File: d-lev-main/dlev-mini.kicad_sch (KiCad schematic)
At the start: 41 parts, among them J1 Conn_01x12_MountingPin, J3 S8B-PH-SM4-TB, J4 S8B-PH-SM4-TB, J5 Conn_01x06_MountingPin, Q3 BSS138, Q4 BSS138, Q5 BSS138, U2 AMS1117-3.3, U4 25LCxxx

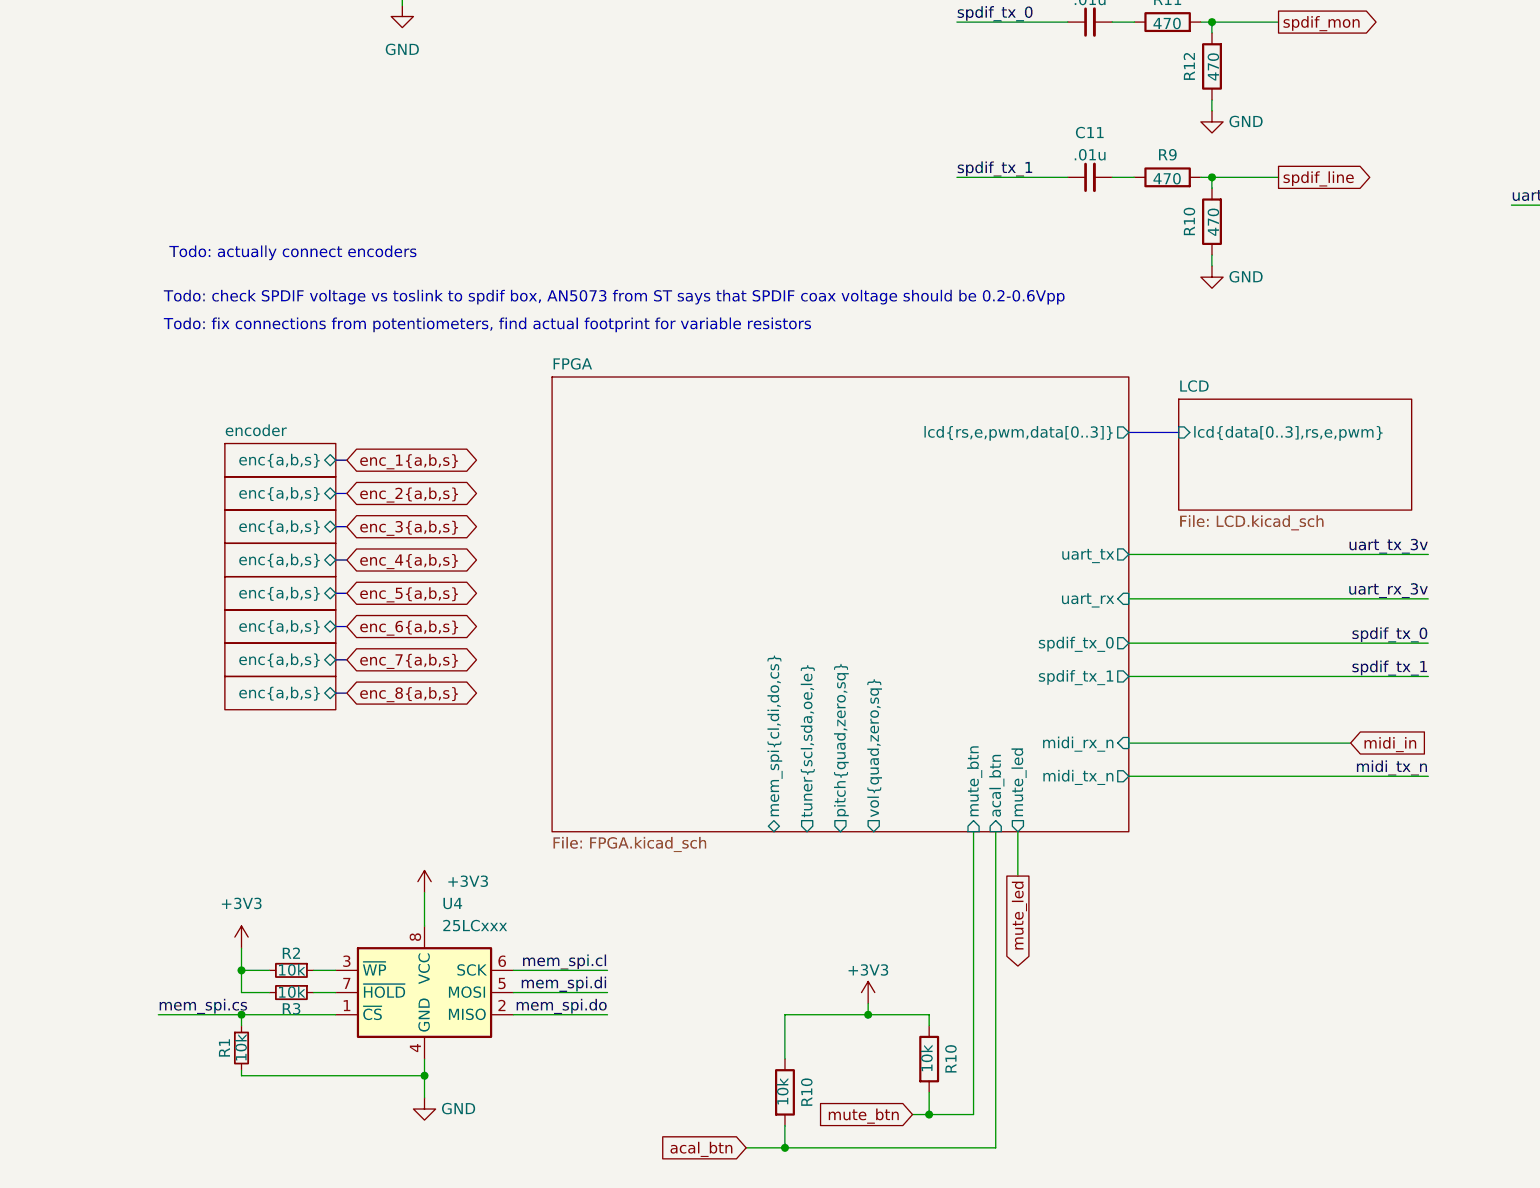
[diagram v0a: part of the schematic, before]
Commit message: start routing
* add simple knob model
* place encoders
* change display to use SMT female headers and SMTSO screw holes
* rotate fpga model 90 degrees
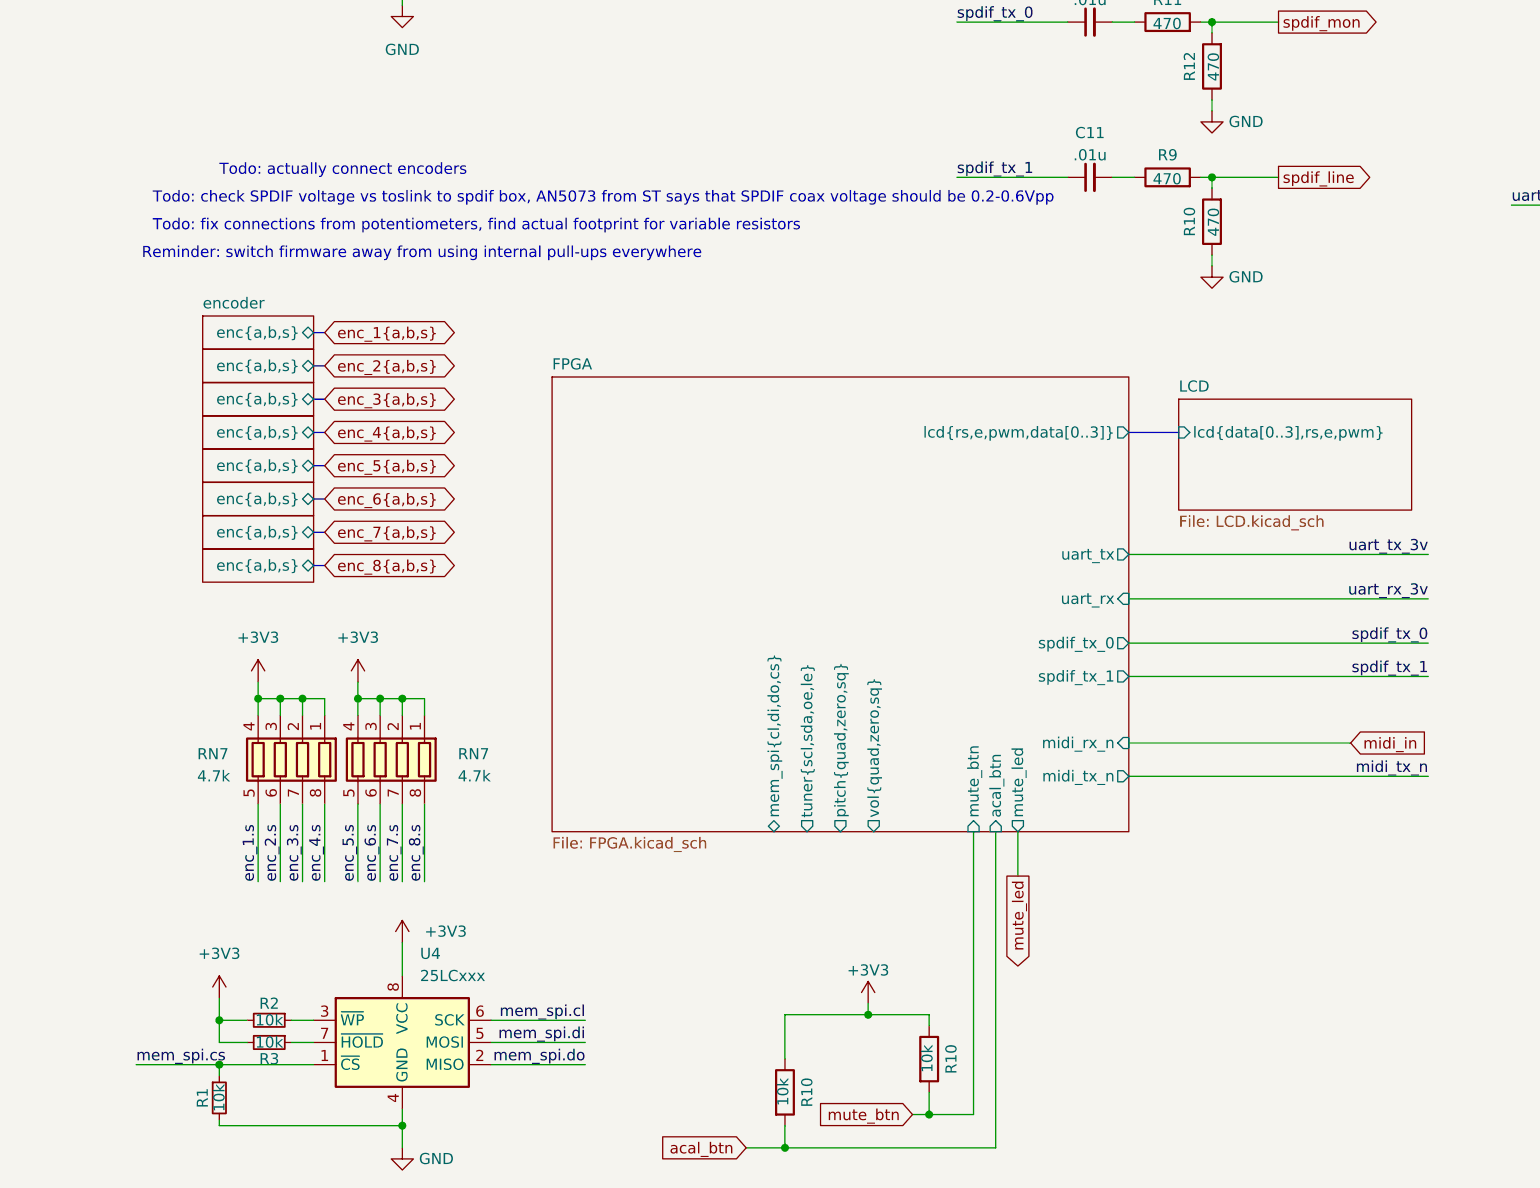
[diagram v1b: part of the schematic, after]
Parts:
- added RN7 (x2): 4.7k, Resistor_SMD:R_Array_Concave_4x0603, symbol Device:R_Pack04
- C11, C9: footprint Capacitor_SMD:C_0805_2012Metric_Pad1.18x1.45mm_HandSolder -> Capacitor_SMD:C_0603_1608Metric
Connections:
- net +3V3: now also RN7.1 (R1.1), RN7.1 (R1.1), RN7.2 (R2.1), RN7.2 (R2.1), RN7.3 (R3.1), RN7.3 (R3.1), RN7.4 (R4.1), RN7.4 (R4.1)
- new net enc_1.s: RN7.5 (R4.2)
- new net enc_2.s: RN7.6 (R3.2)
- new net enc_3.s: RN7.7 (R2.2)
- new net enc_4.s: RN7.8 (R1.2)
- new net enc_5.s: RN7.5 (R4.2)
- new net enc_6.s: RN7.6 (R3.2)
- new net enc_7.s: RN7.7 (R2.2)
- new net enc_8.s: RN7.8 (R1.2)
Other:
- note added: "Reminder: switch firmware away from using internal pull-ups everywhere"
- moved on the sheet: R1, R2, R3, U4

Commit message: many changes to pcb
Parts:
- renumbered C7 to C17, C8 to C18
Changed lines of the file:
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@@
   (symbol (lib_id "Device:C_Small") (at 125.095 62.865 90) (unit 1)
     (in_bom yes) (on_board yes) (dnp no) (fields_autoplaced)
-    (property "Reference" "C9" (at 125.1013 57.785 90)
-      (effects (font (size 1.27 1.27)))
-    )
-    (property "Value" ".01u" (at 125.1013 60.325 90)
+    (property "Reference" "C9" (at 125.1013 57.15 90)
+      (effects (font (size 1.27 1.27)))
+    )
+    (property "Value" ".01u" (at 125.1013 59.69 90)
       (effects (font (size 1.27 1.27)))
     )
@@
         )
         (path "/eb5e8bfd-9871-4528-bf57-58851bf63907"
-          (reference "C9") (unit 1)
+          (reference "C20") (unit 1)
         )
       )
@@
   (symbol (lib_id "Device:C_Polarized_US") (at 33.655 52.07 0) (unit 1)
     (in_bom yes) (on_board yes) (dnp no) (fields_autoplaced)
-    (property "Reference" "C8" (at 37.465 50.8 0)
-      (effects (font (size 1.27 1.27)) (justify left))
-    )
-    (property "Value" "22u" (at 37.465 53.34 0)
+    (property "Reference" "C18" (at 36.83 50.8 0)
+      (effects (font (size 1.27 1.27)) (justify left))
+    )
+    (property "Value" "22u" (at 36.83 53.34 0)
       (effects (font (size 1.27 1.27)) (justify left))
     )
@@
       (project "dlev-mini"
         (path "/eb5e8bfd-9871-4528-bf57-58851bf63907"
-          (reference "C8") (unit 1)
+          (reference "C18") (unit 1)
         )
       )
@@
   (symbol (lib_id "Device:C_Small") (at 125.095 80.645 90) (unit 1)
     (in_bom yes) (on_board yes) (dnp no) (fields_autoplaced)
-    (property "Reference" "C11" (at 125.1013 75.565 90)
-      (effects (font (size 1.27 1.27)))
-    )
-    (property "Value" ".01u" (at 125.1013 78.105 90)
+    (property "Reference" "C11" (at 125.1013 74.93 90)
+      (effects (font (size 1.27 1.27)))
+    )
+    (property "Value" ".01u" (at 125.1013 77.47 90)
       (effects (font (size 1.27 1.27)))
     )
@@
         )
         (path "/eb5e8bfd-9871-4528-bf57-58851bf63907"
-          (reference "C11") (unit 1)
+          (reference "C19") (unit 1)
         )
       )
@@
   (symbol (lib_id "Device:C_Polarized_US") (at 59.055 52.07 0) (unit 1)
     (in_bom yes) (on_board yes) (dnp no) (fields_autoplaced)
-    (property "Reference" "C7" (at 62.865 50.8 0)
+    (property "Reference" "C17" (at 62.865 50.8 0)
       (effects (font (size 1.27 1.27)) (justify left))
     )
@@
       (project "dlev-mini"
         (path "/eb5e8bfd-9871-4528-bf57-58851bf63907"
-          (reference "C7") (unit 1)
-        )
-      )
+          (reference "C17") (unit 1)
+        )
+      )

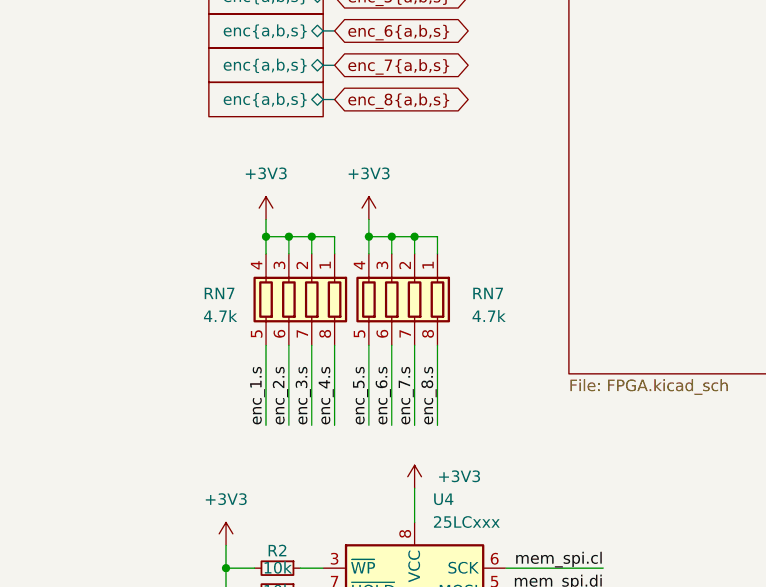
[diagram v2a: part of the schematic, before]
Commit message: Switch from Rpacks to 0603 pull resistors
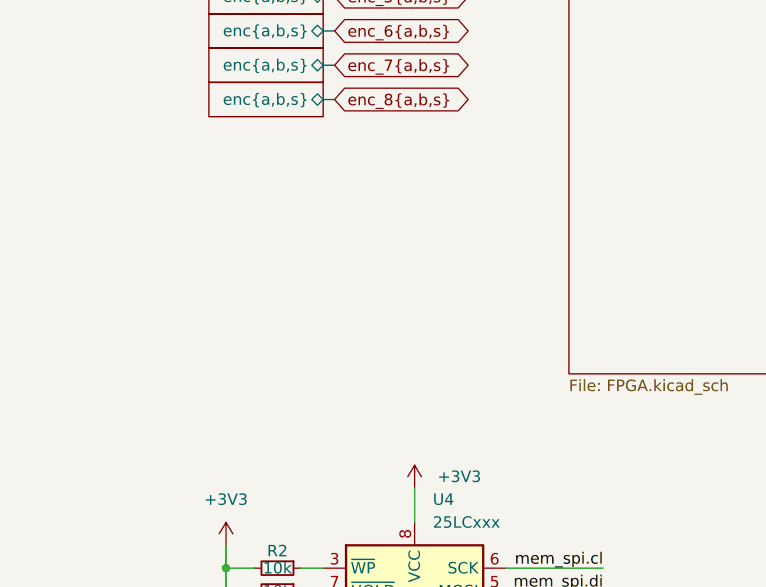
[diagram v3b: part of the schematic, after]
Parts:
- removed RN7 (x2): 4.7k, Resistor_SMD:R_Array_Concave_4x0603, symbol Device:R_Pack04

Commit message: more minor pusharounds and updates
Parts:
- added Q2: BSS138, Package_TO_SOT_SMD:SOT-23, symbol Transistor_FET:BSS138
- added R10: 220, Resistor_SMD:R_0805_2012Metric_Pad1.20x1.40mm_HandSolder, symbol Device:R
- added R10 (x2): 10k, Resistor_SMD:R_0805_2012Metric_Pad1.20x1.40mm_HandSolder, symbol Device:R
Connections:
- net +3V3: now also Q2.1 (G), R10.2
- net +5V: now also R10.2
- net midi_in: now also R10.1
- new net: Q2.3 (D), R10.1, R10.2
- new net midi_rx_n: Q2.2 (S), R10.1
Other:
- sheet LCD ports: added lcd{rs,e,pwm,data[0..3]}; removed lcd{data[0..3],rs,e,pwm}
- moved on the sheet: Q3, Q4, Q5, R10

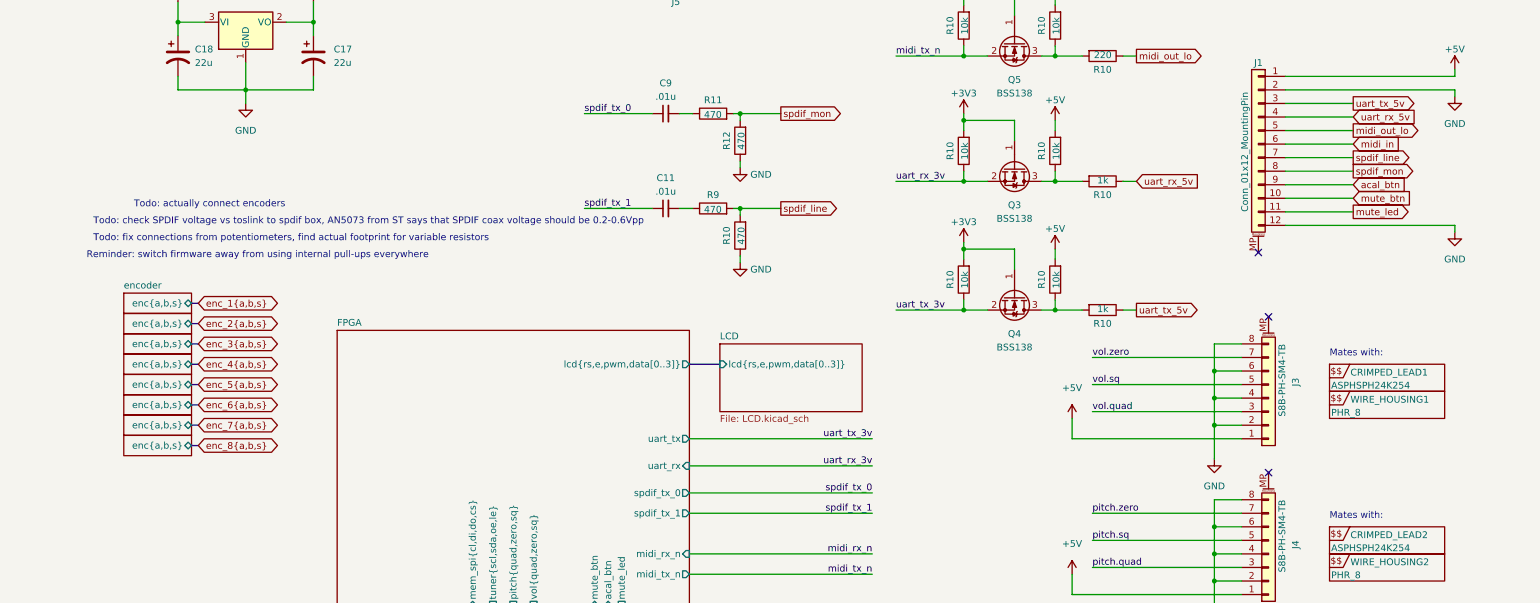
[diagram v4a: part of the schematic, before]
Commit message: Pinned out FPGA and rearranged encoders again
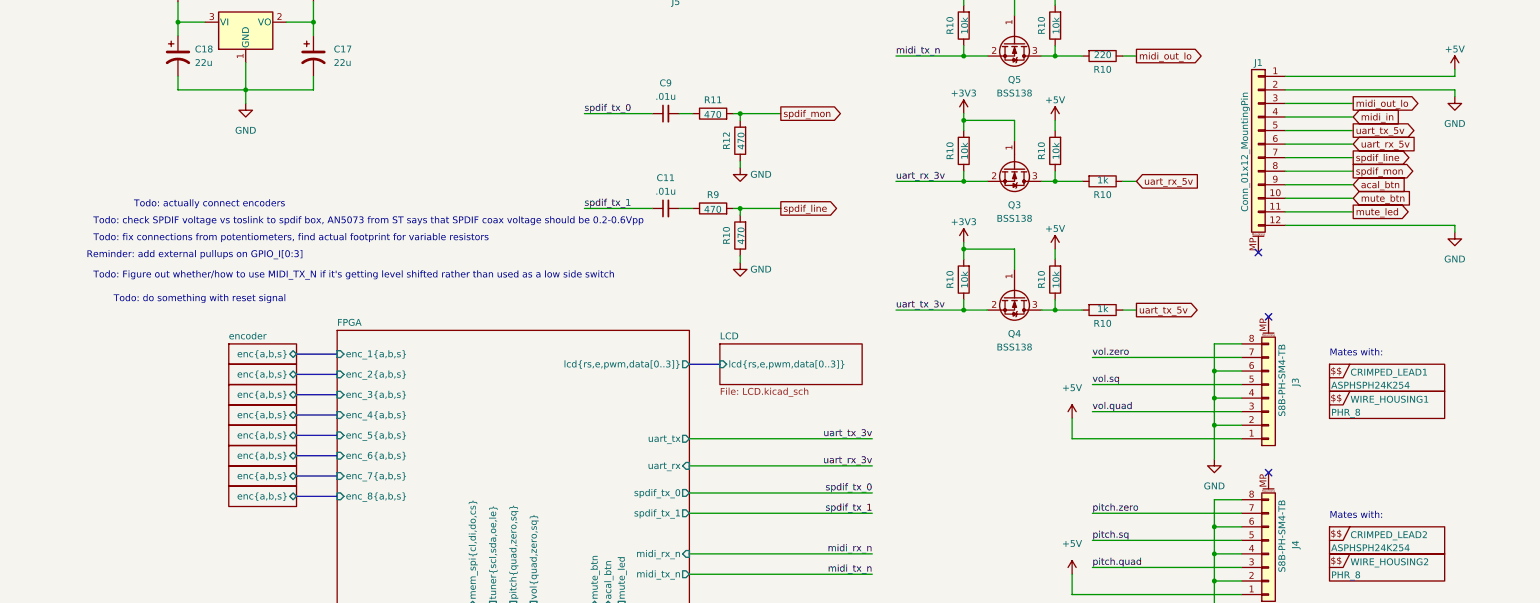
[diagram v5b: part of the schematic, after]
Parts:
- R1, R10, R11, R12, R2, R3, R9: footprint Resistor_SMD:R_0805_2012Metric_Pad1.20x1.40mm_HandSolder -> Resistor_SMD:R_0603_1608Metric
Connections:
- net midi_in: now also J1.4 (Pin_4); no longer J1.6 (Pin_6)
- net midi_out_lo: now also J1.3 (Pin_3); no longer J1.5 (Pin_5)
- net uart_rx_5v: now also J1.6 (Pin_6); no longer J1.4 (Pin_4)
- net uart_tx_5v: now also J1.5 (Pin_5); no longer J1.3 (Pin_3)
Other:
- sheet FPGA ports: added enc_1{a,b,s}, enc_2{a,b,s}, enc_3{a,b,s}, enc_4{a,b,s}, enc_5{a,b,s}, enc_6{a,b,s}, enc_7{a,b,s}, enc_8{a,b,s}; removed none
- note added: "Reminder: add external pullups on GPIO_I[0:3]"
- note added: "Todo: Figure out whether/how to use MIDI_TX_N if it's getting level shifted rather than used as a low side switch"
- note added: "Todo: do something with reset signal"
- note removed: "Reminder: switch firmware away from using internal pull-ups everywhere"
